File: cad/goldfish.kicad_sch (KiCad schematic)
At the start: 26 parts, among them J1 USB_C_Receptacle_USB2.0, J2 Conn_01x02, J3 Conn_01x12, J4 Conn_01x12, J5 Conn_01x05, U1 ATmega32U4-M, U2 USBLC6-2P6, X1 16MHz

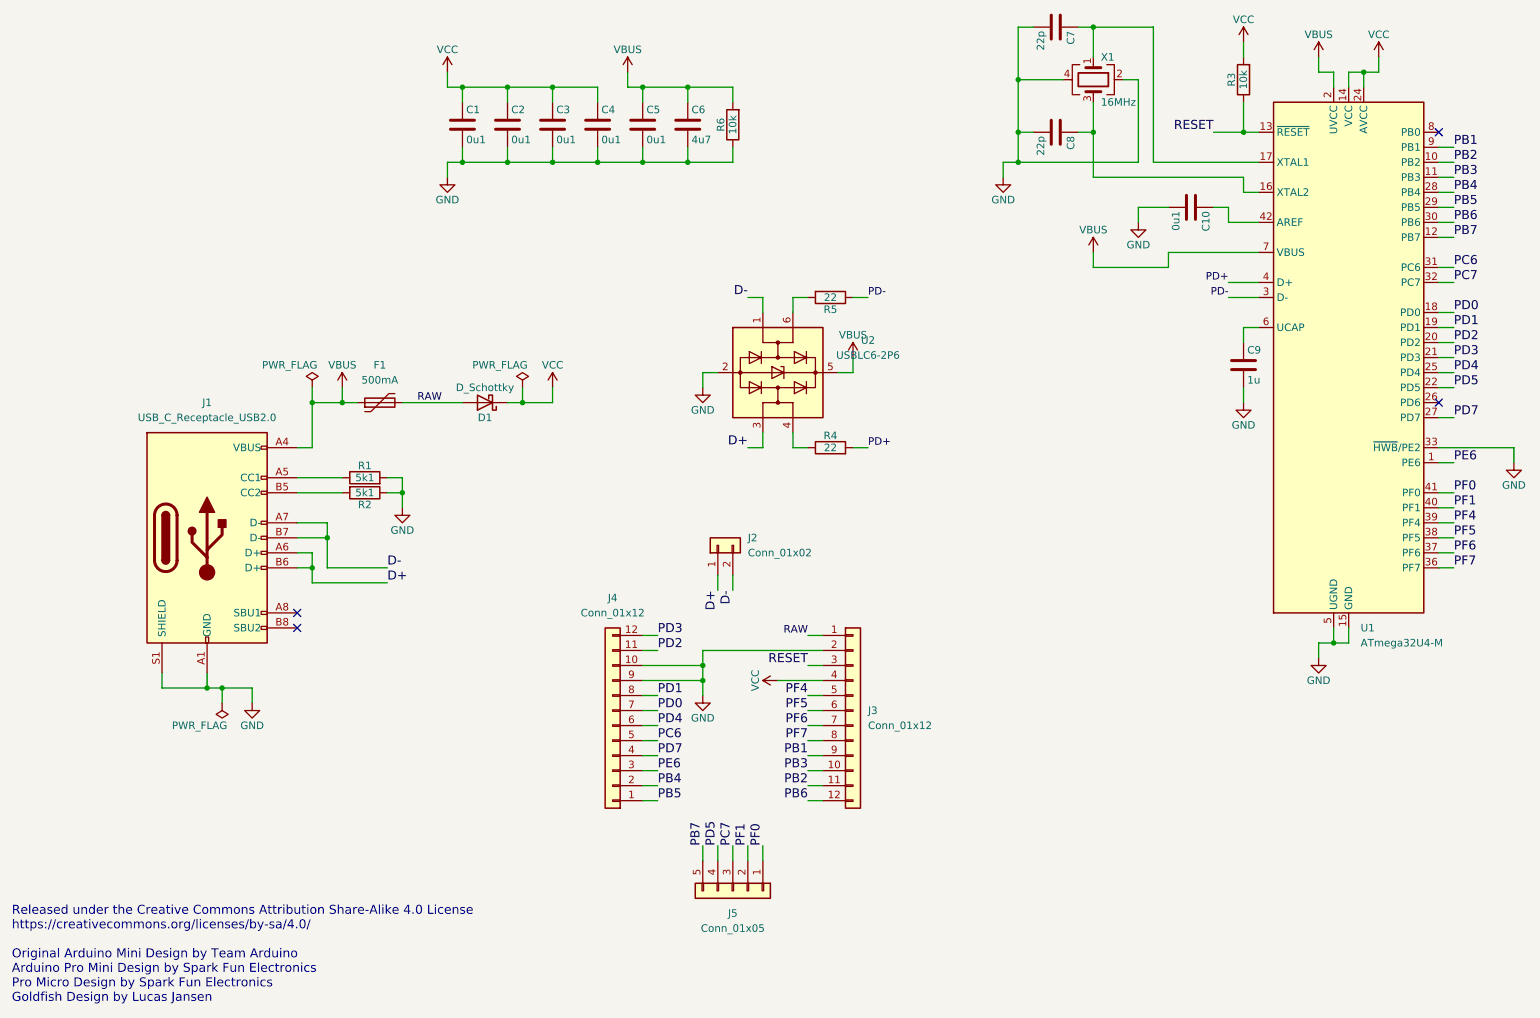
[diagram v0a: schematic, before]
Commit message: corrected front silkscreens and added schematic PDF files
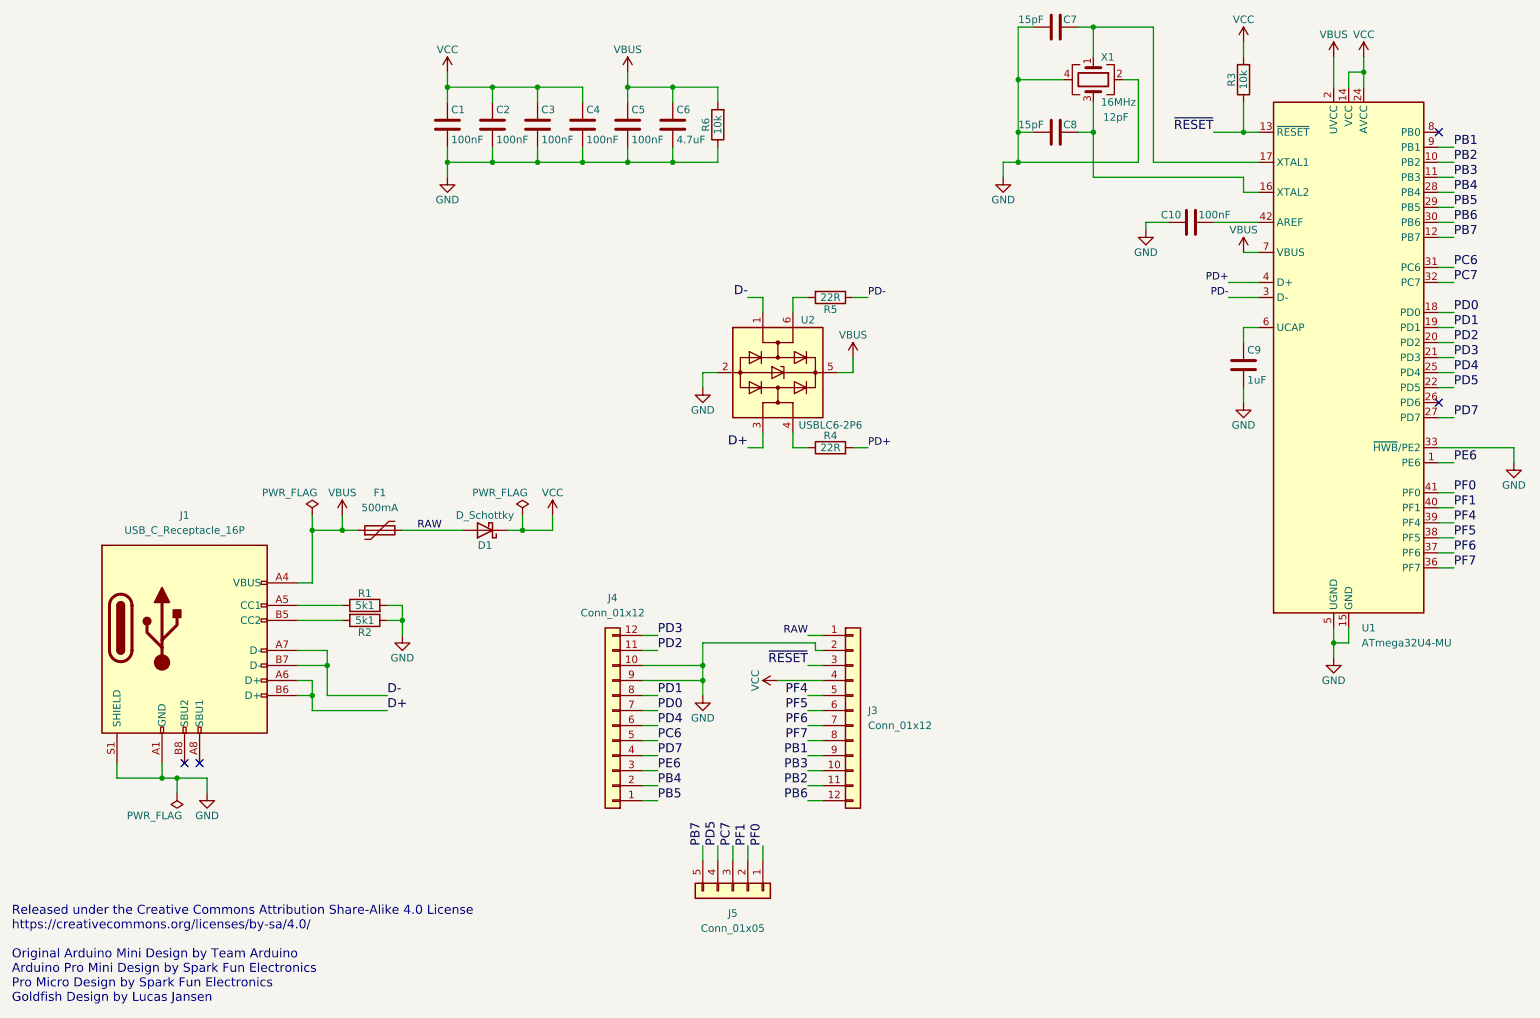
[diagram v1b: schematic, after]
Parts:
- removed J1: USB_C_Receptacle_USB2.0, Molex 216990_GCT USB45xx_HRO TYPE-C-31-M-13x:Molex-216990_GCT-USB45xx_HRO-TYPE-C-31-M-13x, symbol Connector:USB_C_Receptacle_USB2.0
- removed J2: Conn_01x02, Goldfish Pins:Pins_USB, symbol Connector_Generic:Conn_01x02
- added J1: USB_C_Receptacle_16P, TYPE-610-1.6-T3, symbol goldfish_v2:USB_C_Receptacle_16P_TYPE-610-1.6-T3
- C1, C10, C2, C3, C4, C5: value 0u1 -> 100nF; footprint Capacitor_SMD:C_0603_1608Metric -> Capacitor_SMD:C_0402_1005Metric; symbol Device:C -> goldfish_v2:C; Dielectric (none) -> X7R; JLCPCB (none) -> C363530; MPN (none) -> FN15X104J160PNG; Tolerance (none) -> 5%
- C6: value 4u7 -> 4.7uF; footprint Capacitor_SMD:C_0603_1608Metric -> Capacitor_SMD:C_0805_2012Metric; symbol Device:C -> goldfish_v2:C; Dielectric (none) -> X5R; JLCPCB (none) -> C384657; MPN (none) -> TT21X475K160CT; Tolerance (none) -> 10%
- C7, C8: value 22p -> 15pF; footprint Capacitor_SMD:C_0603_1608Metric -> Capacitor_SMD:C_0402_1005Metric; symbol Device:C -> goldfish_v2:C; Dielectric (none) -> C0G; JLCPCB (none) -> C140684; MPN (none) -> C0402C0G150G500NTB; Tolerance (none) -> 2%
- C9: value 1u -> 1uF; symbol Device:C -> goldfish_v2:C; Dielectric (none) -> X5R; JLCPCB (none) -> C3015156; MPN (none) -> CSA0603X5R105K160JT
- D1: symbol Device:D_Schottky -> goldfish_v2:D_Schottky; JLCPCB (none) -> C908229; MPN (none) -> DSK24
- F1: footprint Fuse:Fuse_0805_2012Metric -> Fuse:Fuse_1206_3216Metric; symbol Device:Polyfuse -> goldfish_v2:Polyfuse; JLCPCB (none) -> C492011; MPN (none) -> SMD1206P050TF/24
- J3, J4: footprint Goldfish Pins:Pins_x12_Castellated -> Goldfish_V2:Pins_x12; symbol Connector_Generic:Conn_01x12 -> goldfish_v2:Conn_01x12
- J5: footprint Goldfish Pins:Pins_x05_Castellated -> Goldfish_V2:Pins_x05; symbol Connector_Generic:Conn_01x05 -> goldfish_v2:Conn_01x05
- R1, R2: symbol Device:R -> goldfish_v2:R; JLCPCB (none) -> C209245; MPN (none) -> RMS06JT512
- R3, R6: footprint Resistor_SMD:R_0603_1608Metric -> Resistor_SMD:R_0402_1005Metric; symbol Device:R -> goldfish_v2:R; JLCPCB (none) -> C851039; MPN (none) -> AT0402BRD074K7L
- R4, R5: value 22 -> 22R; footprint Resistor_SMD:R_0603_1608Metric -> Resistor_SMD:R_0402_1005Metric; symbol Device:R -> goldfish_v2:R; JLCPCB (none) -> C284431; MPN (none) -> ARG02FTC22R1
- U1: value ATmega32U4-M -> ATmega32U4-MU; symbol MCU_Microchip_ATmega:ATmega32U4-M -> goldfish_v2:ATmega32U4-M; JLCPCB (none) -> C112161; MPN (none) -> ATmega32U4-MU
- U2: symbol Power_Protection:USBLC6-2P6 -> goldfish_v2:USBLC6-2P6; JLCPCB (none) -> C15999; MPN (none) -> USBLC6-2P6
- X1: symbol Device:Crystal_GND24 -> goldfish_v2:Crystal_GND24; JLCPCB (none) -> C251610; Load Cap (none) -> 12pF; MPN (none) -> 7U16000E12UCG; Tolerance (none) -> 10ppm
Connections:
- net D+: now also J1.A6 (D+), J1.B6 (D+)
- net D-: now also J1.A7 (D-), J1.B7 (D-)
- net GND: now also J1.A1 (GND), J1.A12 (GND), J1.B1 (GND), J1.B12 (GND), J1.S1 (SHIELD)
- net VBUS: now also J1.A4 (VBUS), J1.A9 (VBUS), J1.B4 (VBUS), J1.B9 (VBUS)
- net at R2.2: now also J1.B5 (CC2)
- net at R1.1: now also J1.A5 (CC1)
- net RESET renamed ~{RESET}
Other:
- moved on the sheet: C1, C10, C2, C3, C4, C5, C6, D1, F1, R1, R2, R6
